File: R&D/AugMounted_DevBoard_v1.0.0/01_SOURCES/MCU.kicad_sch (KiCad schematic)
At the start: 7 parts, among them J1 J_TYPE-C-31-M-13, U1 ESP32-S3-WROOM-1U-N16R8, U9 U_VCNL4040M3OE

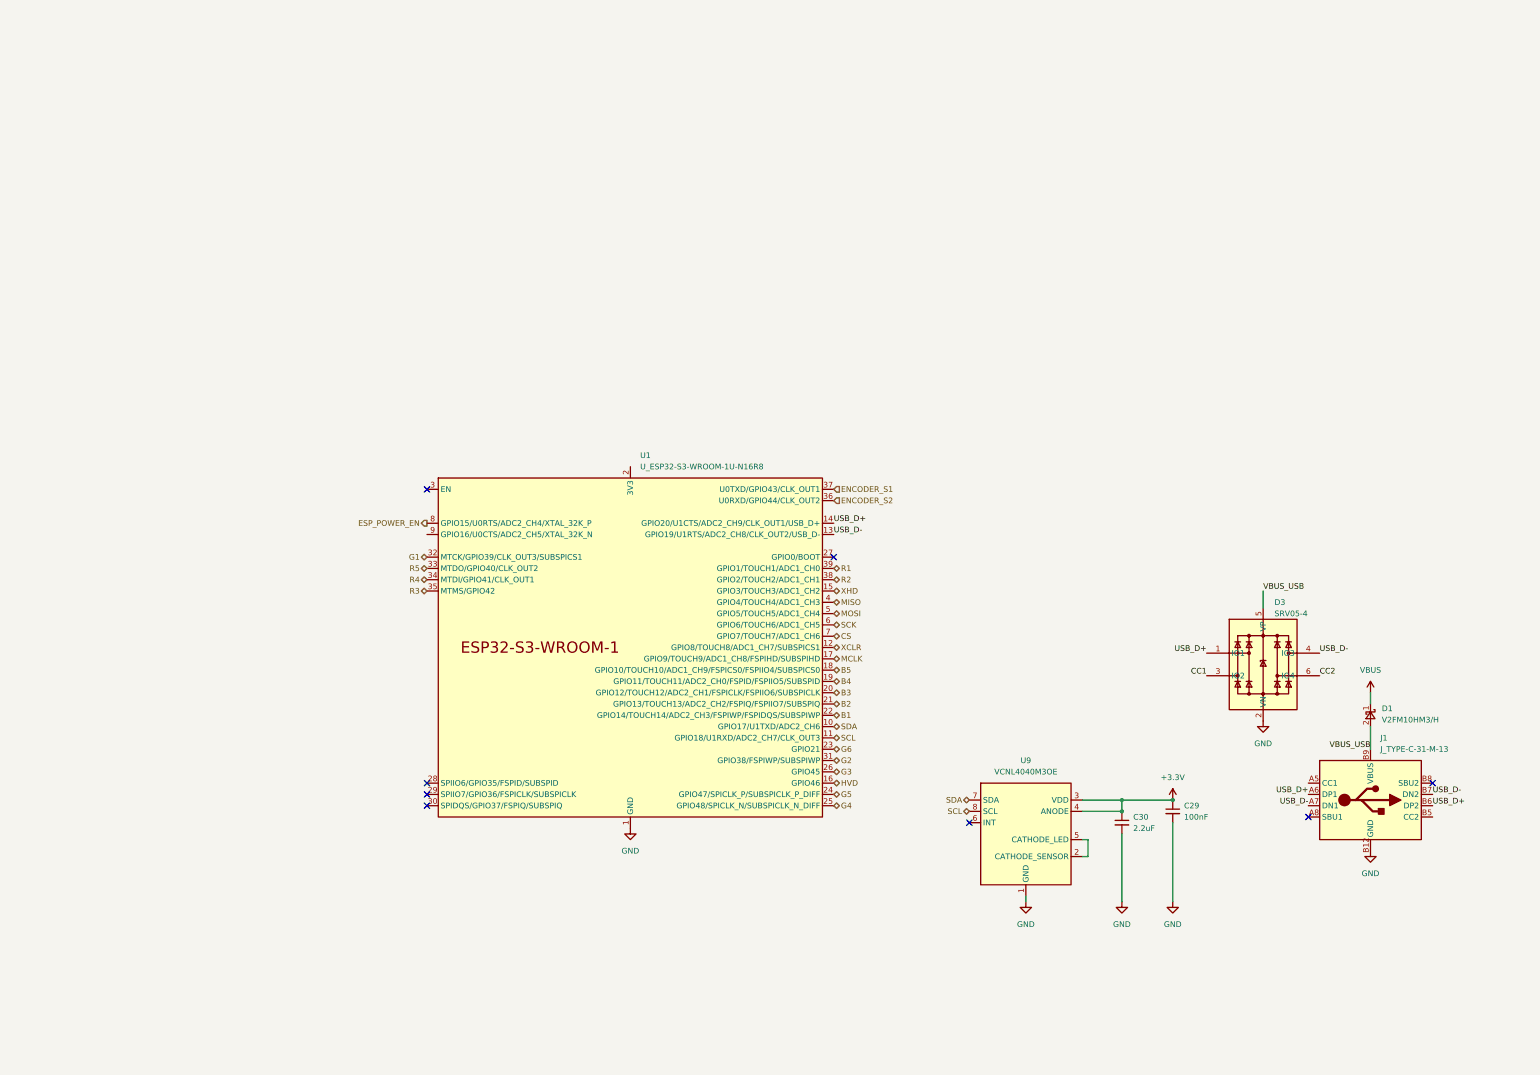
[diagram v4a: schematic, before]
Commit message: Schematic done
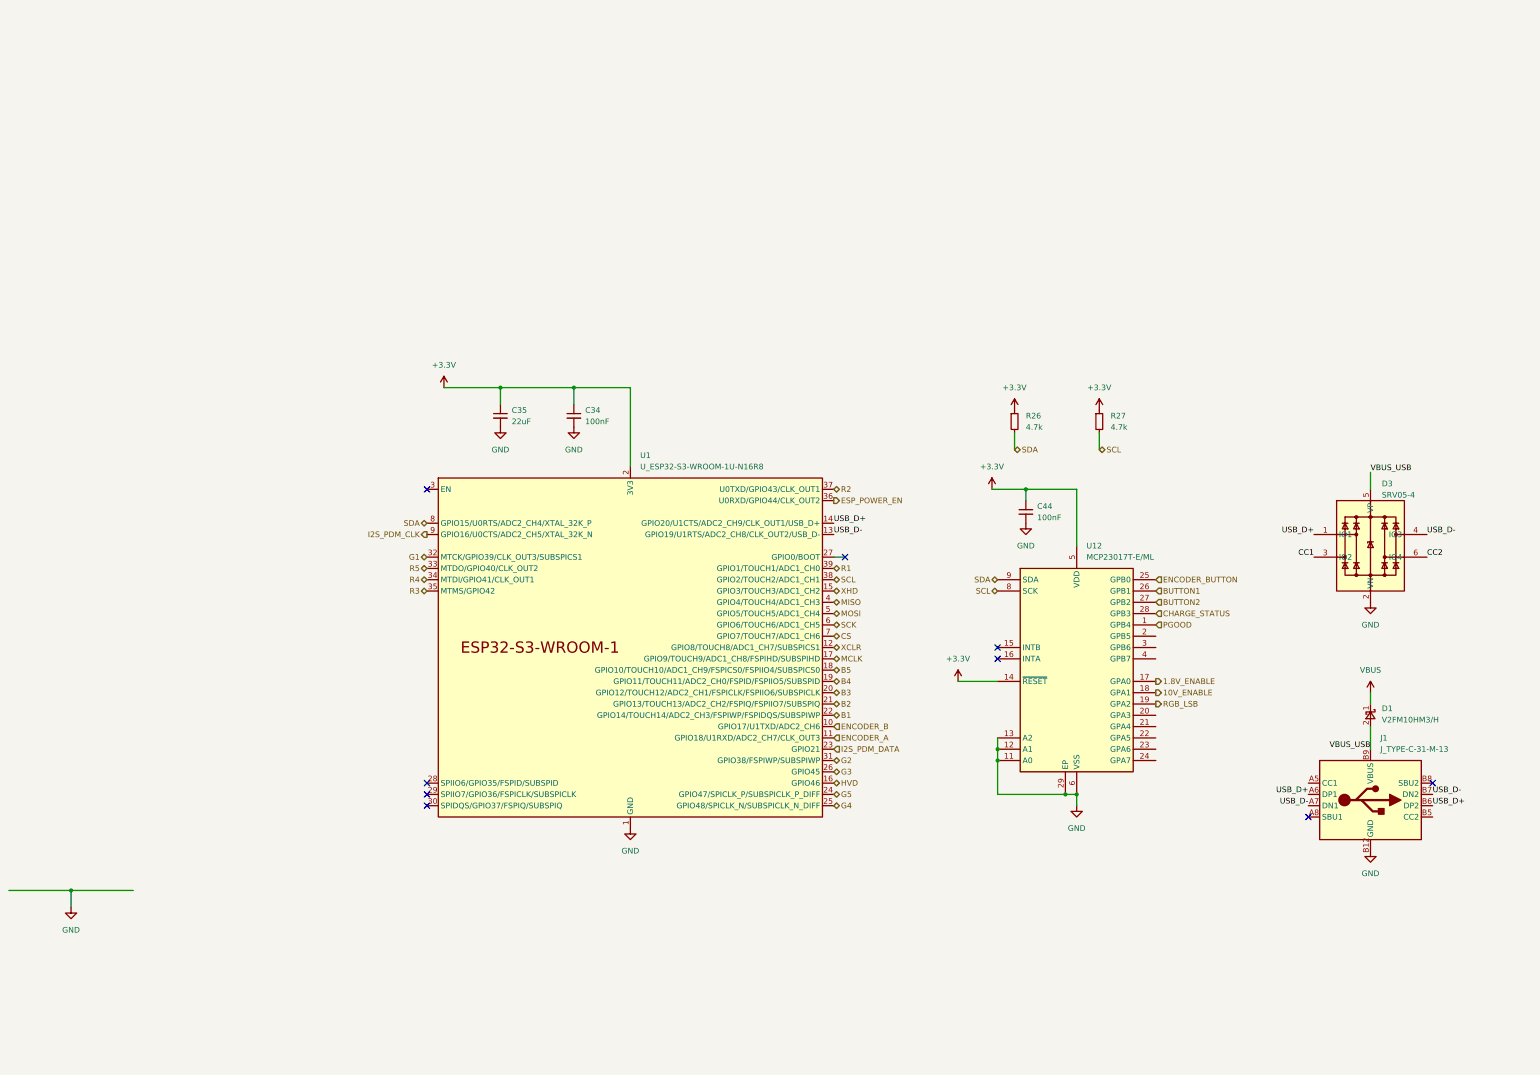
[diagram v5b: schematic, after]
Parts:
- removed C29: C_0603_100nF_100V_X7R_10%, .mounted-lib:C_0603_1608Metric, symbol .mounted-lib:C_0603_100nF_100V_X7R_10%
- removed C30: C_0603_2.2uF_10V_X7R_10%, .mounted-lib:C_0603_1608Metric, symbol .mounted-lib:C_0603_2.2uF_10V_X7R_10%
- removed U9: U_VCNL4040M3OE, .mounted-lib:VCNL4040_4X2X1.1_VISHAY, symbol .mounted-lib:U_VCNL4040M3OE
- added C34, C44: C_0603_100nF_100V_X7R_10%, .mounted-lib:C_0603_1608Metric, symbol .mounted-lib:C_0603_100nF_100V_X7R_10%
- added C35: C_0805_22uF_10V_XR7_20%, .mounted-lib:C_0805_1608Metric, symbol .mounted-lib:C_0805_22uF_10V_XR7_20%
- added R26, R27: R_0603_4.7k_1%_0.1W, .mounted-lib:R_0603_1608Metric, symbol .mounted-lib:R_0603_4.7k_1%_0.1W
- added U12: U_MCP23017T-E/ML, .mounted-lib:QFN-28-1EP_6x6mm_P0.65mm_EP4.25x4.25mm_MICROCHIP, symbol .mounted-lib:U_MCP23017T-E/ML
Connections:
- net ENCODER_S1 is gone; now on net R2: U1.37 (U0TXD/GPIO43/CLK_OUT1)
- net ENCODER_S2 is gone; now on net ESP_POWER_EN: U1.36 (U0RXD/GPIO44/CLK_OUT2)
- net +3.3V: now also U1.2 (3V3), C34.1, C35.1, C44.1, R26.1, R27.1, U12.14 (~{RESET}), U12.5 (VDD)
- net ESP_POWER_EN: no longer U1.8 (GPIO15/U0RTS/ADC2_CH4/XTAL_32K_P)
- net GND: now also C34.2, C35.2, C44.2, U12.11 (A0), U12.12 (A1), U12.13 (A2), U12.29 (EP), U12.6 (VSS)
- net R2: no longer U1.38 (GPIO2/TOUCH2/ADC1_CH1)
- net SCL: now also U1.38 (GPIO2/TOUCH2/ADC1_CH1), R27.2, U12.8 (SCK); no longer U1.11 (GPIO18/U1RXD/ADC2_CH7/CLK_OUT3)
- net SDA: now also U1.8 (GPIO15/U0RTS/ADC2_CH4/XTAL_32K_P), R26.2, U12.9 (SDA); no longer U1.10 (GPIO17/U1TXD/ADC2_CH6)
- net I2S_PDM_CLK: now reaches U1.9 (GPIO16/U0CTS/ADC2_CH5/XTAL_32K_N)
- net G6 renamed I2S_PDM_DATA
- new net 1.8V_ENABLE: U12.17 (GPA0)
- new net 10V_ENABLE: U12.18 (GPA1)
- new net BUTTON1: U12.26 (GPB1)
- new net BUTTON2: U12.27 (GPB2)
- new net CHARGE_STATUS: U12.28 (GPB3)
- new net ENCODER_A: U1.11 (GPIO18/U1RXD/ADC2_CH7/CLK_OUT3)
- new net ENCODER_B: U1.10 (GPIO17/U1TXD/ADC2_CH6)
- new net ENCODER_BUTTON: U12.25 (GPB0)
- new net PGOOD: U12.1 (GPB4)
- new net RGB_LSB: U12.19 (GPA2)
- no-connect marks 8 -> 9
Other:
- moved on the sheet: D3

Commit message: First revision of the layout
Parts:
- renumbered C35 to C201, C34 to C202, C44 to C203, D3 to D201, D1 to D202, J1 to J201, R26 to R201, R27 to R202, U12 to U202, U1 to U?
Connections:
- net CC1: now also D201.4 (IO3); no longer D201.3 (IO2)
- net USB_D-: now also D201.3 (IO2); no longer D201.4 (IO3)

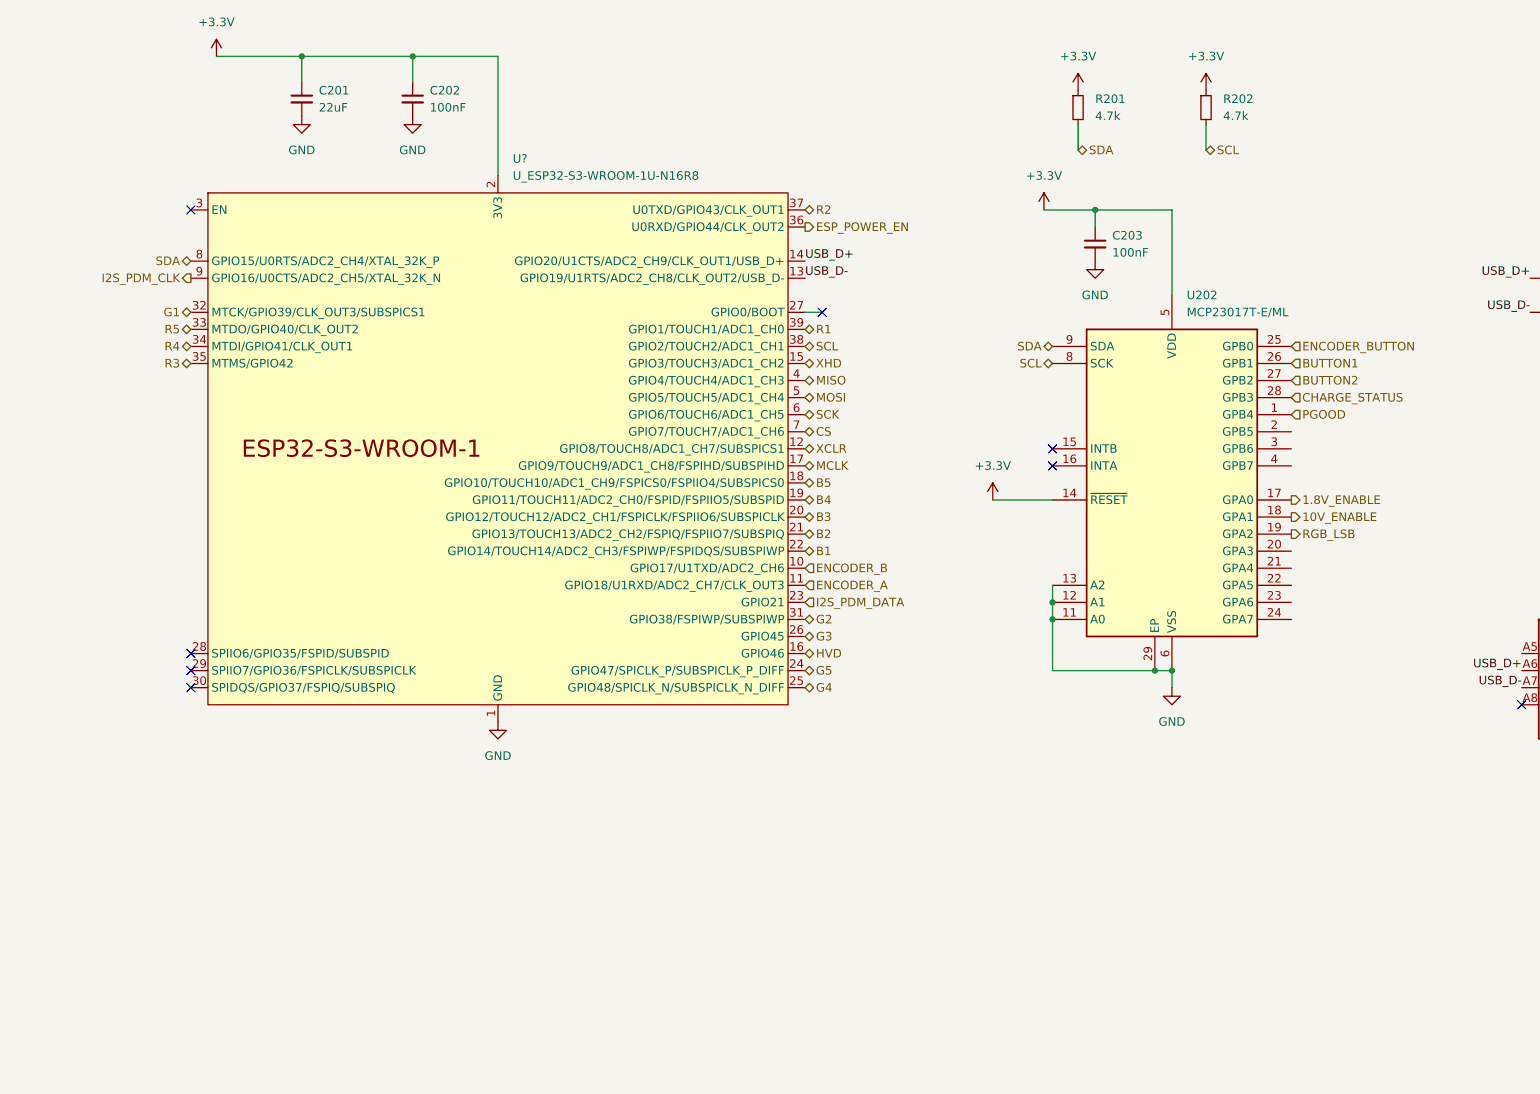
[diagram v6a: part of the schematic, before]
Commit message: Changed layout to a banana shape
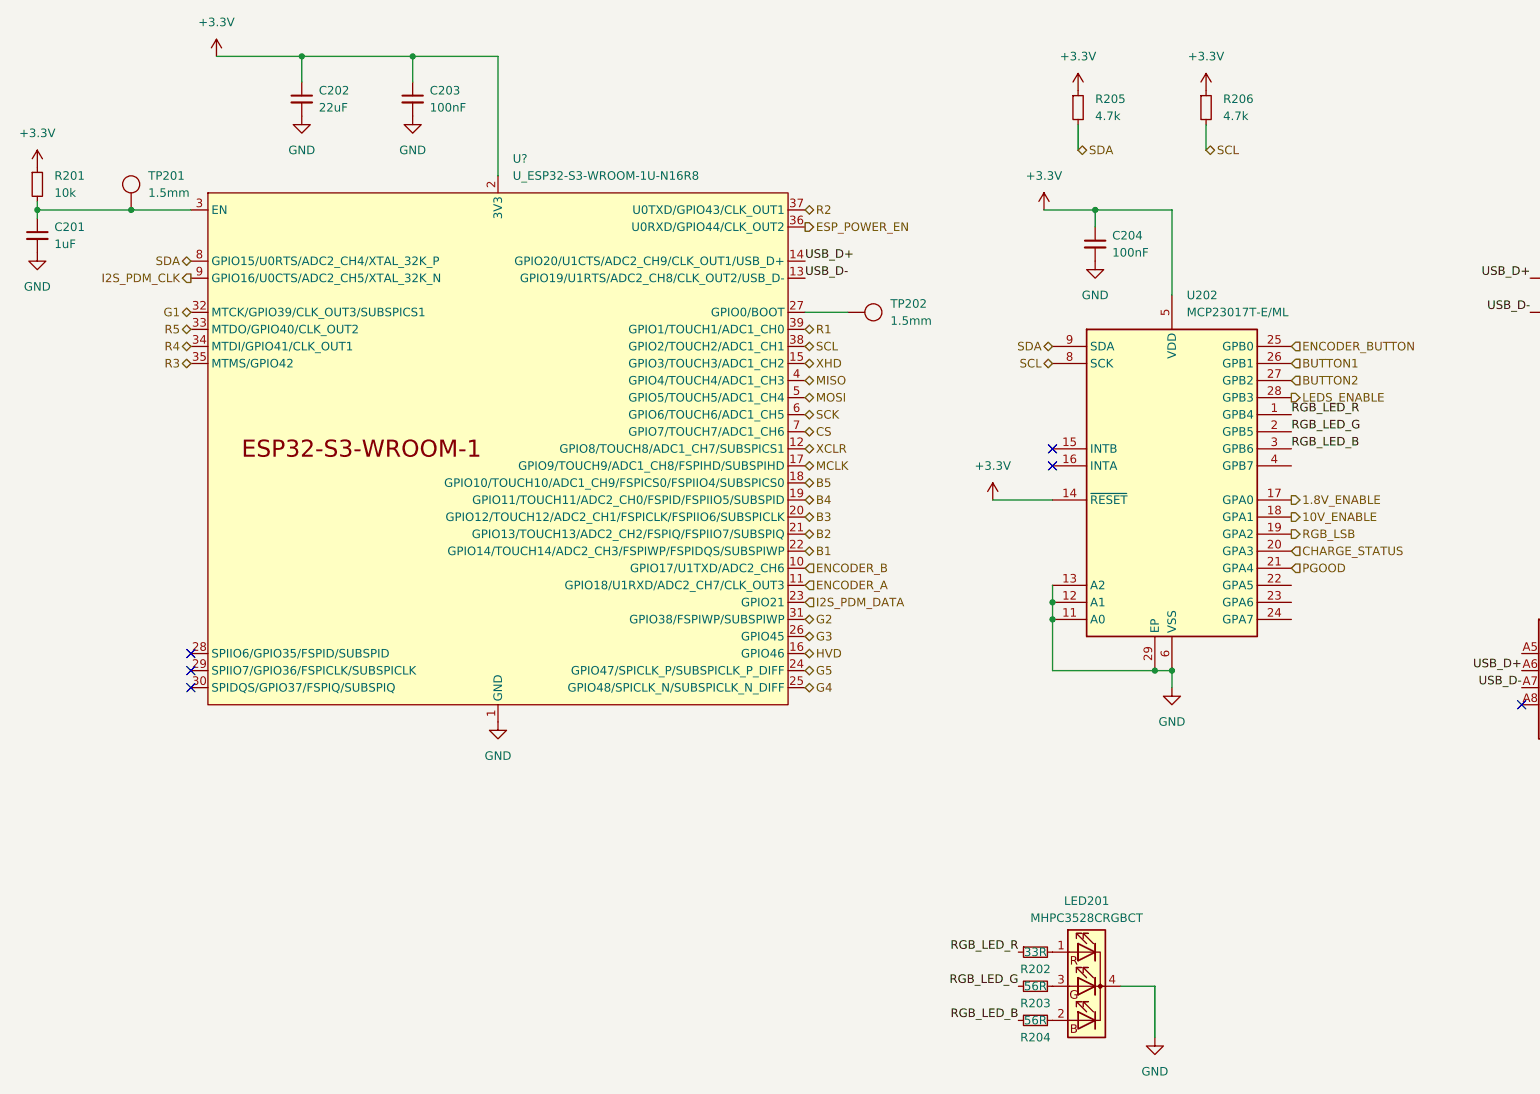
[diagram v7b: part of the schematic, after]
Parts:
- added C201: C_0603_1uF_16V_X7R_10%, .mounted-lib:C_0603_1608Metric, symbol .mounted-lib:C_0603_1uF_16V_X7R_10%_1
- added LED201: LED_MHPC3528CRGBCT, .mounted-lib:LED_MHPC3528CRGBCT, symbol .mounted-lib:LED_MHPC3528CRGBCT
- added R201: R_0603_10k_1%_0.1W, .mounted-lib:R_0603_1608Metric, symbol .mounted-lib:R_0603_10k_1%_0.1W
- added R202: R_0603_33R_1%_0.1W, .mounted-lib:R_0603_1608Metric, symbol .mounted-lib:R_0603_33R_1%_0.1W
- added R203, R204: R_0603_56R_1%_0.1W, .mounted-lib:R_0603_1608Metric, symbol .mounted-lib:R_0603_56R_1%_0.1W
- added TP201, TP202: TESTPOINT_1.5MM, .mounted-lib:TESTPOINT_1.5MM, symbol .mounted-lib:TESTPOINT_1.5MM
- renumbered C201 to C202, C202 to C203, C203 to C204, R201 to R205, R202 to R206
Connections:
- net +3.3V: now also R201.1
- net CHARGE_STATUS: now also U202.20 (GPA3); no longer U202.28 (GPB3)
- net GND: now also C201.2, LED201.4 (K)
- net PGOOD: now also U202.21 (GPA4); no longer U202.1 (GPB4)
- net RGB_LED_G: now reaches U202.2 (GPB5)
- net RGB_LED_G: now also R203.2
- net RGB_LED_B: now reaches U202.3 (GPB6)
- net RGB_LED_B: now also R204.2
- net at U?.27 (GPIO0/BOOT): now also TP202.1
- net at U?.3 (EN): now also C201.1, R201.2, TP201.1
- new net: LED201.1 (RA), R202.2
- new net: LED201.2 (GA), R204.1
- new net: LED201.3 (BA), R203.1
- new net LEDS_ENABLE: U202.28 (GPB3)
- new net RGB_LED_R: R202.1, U202.1 (GPB4)
- no-connect marks 9 -> 7
